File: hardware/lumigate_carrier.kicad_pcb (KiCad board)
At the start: 2 copper layers, 82.2 x 28.2 mm, 24 parts, among them J1 XLR-3 DMX out (XLR-328P), J2 USB-C 6P power (TYPE-C 6P), J3 1x10 socket 2.54 (C35445), J4 1x10 socket 2.54 (C35445), U1 ESP32-POE-ISO module (plug-in), U2 SOIC-20W_7.5x12.8mm_P1.27mm, U3 SOT-23-5

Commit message: @ hardware: re-route after USB-C (J2) 180deg orientation fix
J2 footprint needed a 180deg flip so the connector mates with the pads; re-routed
clean (0 unconnected / 0 shorts / 0 edge). Regenerated gerbers/drill/CPL (J2 now
rot 0 in CPL), all on the bottom-left aux origin.

Co-Authored-By: Claude Opus 4.8 <noreply@anthropic.com>
@
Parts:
- moved J2 1.88 mm to (132.2, 108.0), turned to 0 degrees
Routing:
- net +3V3: track 66.7 -> 74.6 mm
- net DMX_RX: track 28.6 -> 33.2 mm, vias 1 -> 0
- net CC1: track 32.7 -> 28.2 mm
- net VBUS_C: track 46.0 -> 41.6 mm, vias 3 -> 0
- net DMX_EN: track 52.1 -> 54.9 mm
- net +5V: track 68.5 -> 66.0 mm, vias 0 -> 1
- net DMX_A: track 46.9 -> 47.9 mm
- net CC2: track 19.5 -> 18.6 mm, vias 2 -> 0
- net DMX_TX: vias 1 -> 0

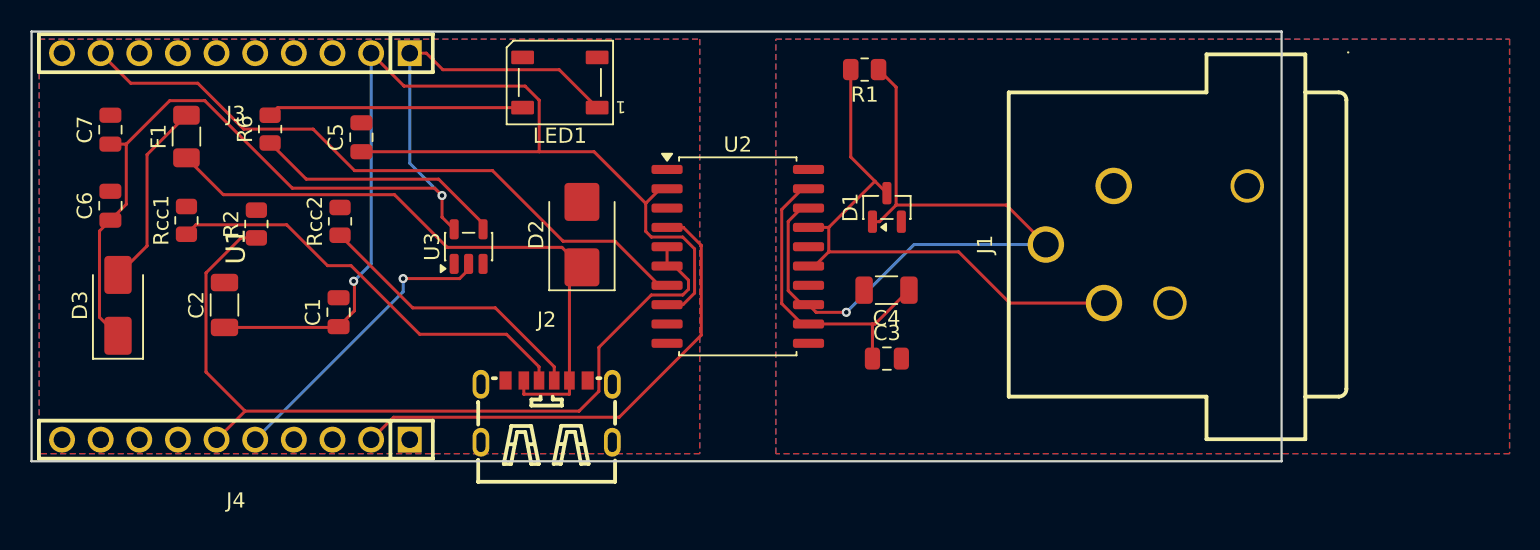
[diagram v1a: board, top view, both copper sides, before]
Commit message: @ hardware: re-route (clean 0/0/0), regenerate fab
Co-Authored-By: Claude Opus 4.8 <noreply@anthropic.com>
@
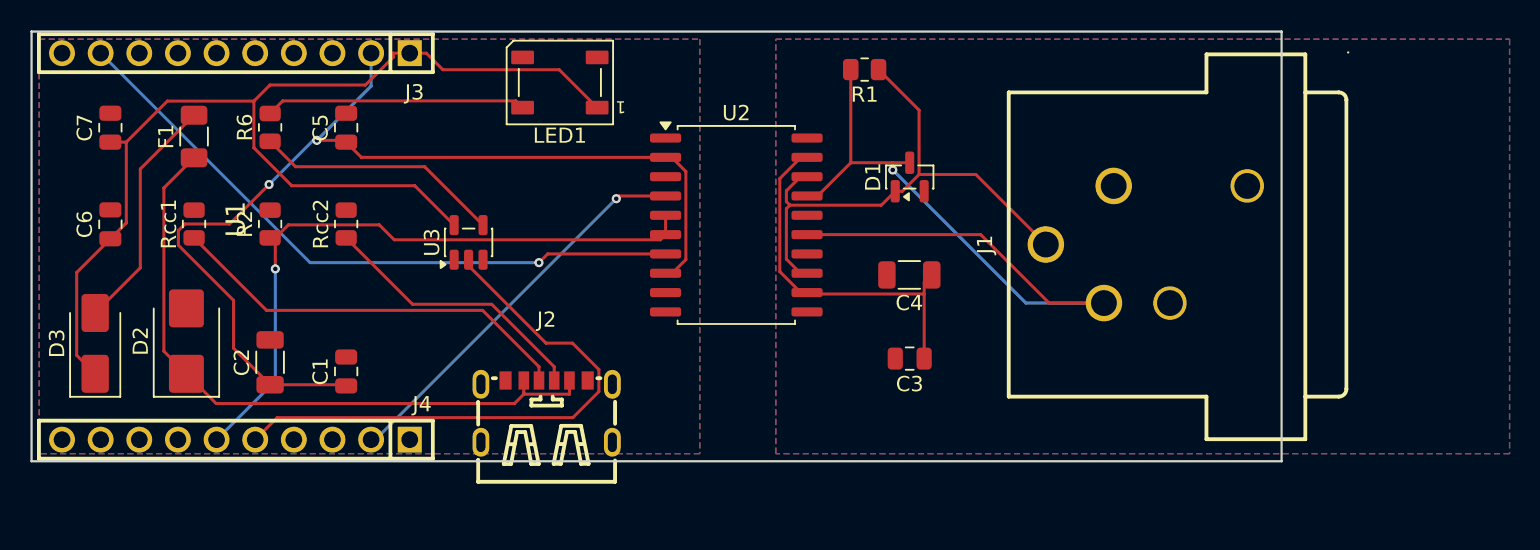
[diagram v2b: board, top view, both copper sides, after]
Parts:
- moved D2 26.9 mm to (108.5, 103.3)
- moved C2 4.82 mm to (114.0, 104.7)
- moved C1 3.93 mm to (119.0, 105.3)
- moved D3 2.92 mm to (102.5, 103.5)
- moved D1 2.50 mm to (156.1, 92.6)
- moved U2 2.07 mm to (144.7, 95.7)
- moved C4 1.80 mm to (156.0, 99.0)
- moved C3 1.50 mm to (156.1, 104.5), turned to 180 degrees
- moved C6 1.22 mm to (103.5, 95.7)
- moved C5 1.18 mm to (119.0, 89.3)
- moved R2 0.90 mm to (114.0, 95.7)
- moved Rcc1 0.55 mm to (109.0, 95.7)
- moved F1 0.50 mm to (109.0, 89.9)
- moved Rcc2 0.44 mm to (119.0, 95.7)
- moved U3 0.28 mm to (127.0, 96.9)
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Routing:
- net RGB_DIN: track 19.5 -> 37.1 mm, vias 1 -> 0
- net DMX_B: track 37.5 -> 53.1 mm, vias 0 -> 1
- net DMX_A: track 47.9 -> 35.7 mm, vias 1 -> 0
- net DMX_EN: track 54.9 -> 43.0 mm, vias 0 -> 1
- net DMX_RX: track 33.2 -> 26.0 mm, vias 0 -> 1
- net +3V3: track 74.6 -> 69.0 mm, vias 1 -> 2
- net +5V: track 66.0 -> 71.5 mm, vias 1 -> 0
- net VISO: track 20.6 -> 24.3 mm
- net VBUS_FUSED: track 12.4 -> 15.7 mm
- net VBUS_C: track 41.6 -> 43.7 mm
- net CC1: track 28.2 -> 27.1 mm
- net DMX_TX: track 43.6 -> 43.1 mm, vias 0 -> 1
